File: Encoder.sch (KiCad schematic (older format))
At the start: 7 parts

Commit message: finalizado enrutado provisional
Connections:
- net D2: now also C16.1, R42.2; no longer C15.1, R40.2
- net D5: now also C15.1, R40.2; no longer C16.1, R42.2
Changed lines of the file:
@@
 	3700 2800 3150 2800
 Connection ~ 3150 2800
+Text GLabel 3700 2800 2    50   Output ~ 0
+D2
 Text GLabel 3700 2700 2    50   Output ~ 0
-D2
-Text GLabel 3700 2800 2    50   Output ~ 0
 D5
 $Bitmap

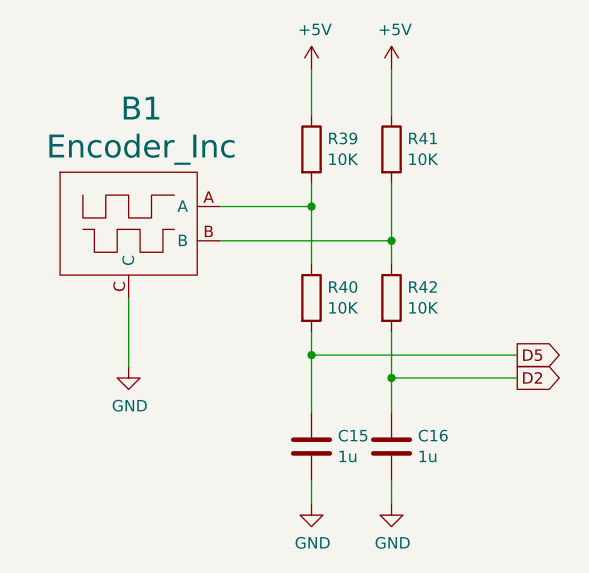
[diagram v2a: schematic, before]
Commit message: corregidos valores en esquema y simbolos corruptos
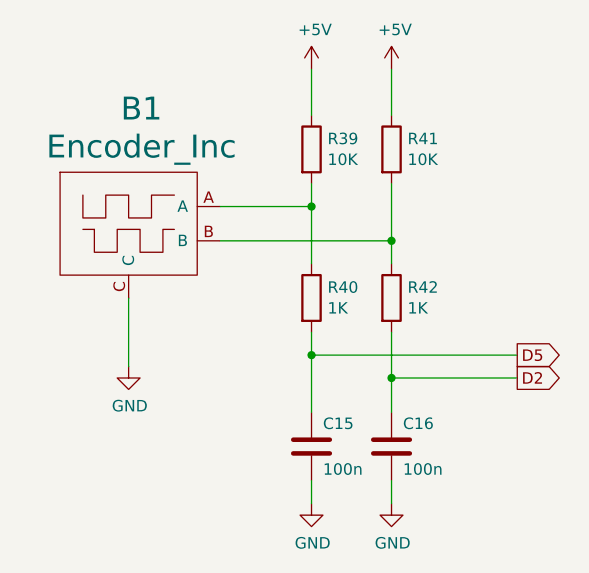
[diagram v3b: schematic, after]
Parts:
- C15: value 1u -> 100n; Ref CL21B105KAFNNNE -> CL21B104KBCNNNC; Ref_Proveedor CL21B105KAFNNNE -> CL21B104KBCNNNC
- C16: value 1u -> 100n; Ref_Proveedor CL21B105KAFNNNE -> CL21B105KAFNNNECL21B104KBCNNNC
- R40, R42: value 10K -> 1K; Ref CRCW080510K0FKEA -> CL21B104KBCNNNC; Ref_Proveedor CRCW080510K0FKEA -> CL21B104KBCNNNC
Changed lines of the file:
@@
 EESchema Schematic File Version 2
+LIBS:Nano_PB-rescue
 LIBS:Interfaces
-LIBS:Nano_PB-rescue
 LIBS:Sensores
 LIBS:power
@@
 LIBS:matriz_led
 LIBS:Pasivos
+LIBS:Reles
 LIBS:Nano_PB-cache
 EELAYER 26 0
@@
 	2000 2450 2000 2750
 $Comp
-L GND #PWR083
+L GND #PWR075
 U 1 1 579DF9A7
 P 2000 2750
-F 0 "#PWR083" H 2000 2500 50  0001 C CNN
+F 0 "#PWR075" H 2000 2500 50  0001 C CNN
 F 1 "GND" H 2005 2577 50  0000 C CNN
 F 2 "" H 2000 2750 50  0000 C CNN
@@
 P 2800 2450
 F 0 "R40" H 2870 2496 50  0000 L CNN
-F 1 "10K" H 2870 2405 50  0000 L CNN
+F 1 "1K" H 2870 2405 50  0000 L CNN
 F 2 "Resistencias:R_0805" V 2730 2450 50  0001 C CNN
 F 3 "" H 2800 2450 50  0000 C CNN
 F 4 "VISHAY" H 4350 1650 60  0001 C CNN "Fabricante"
-F 5 "CRCW080510K0FKEA" H 4350 1650 60  0001 C CNN "Ref"
-F 6 "1/8W" H 4350 1650 60  0001 C CNN "Potencia"
-F 7 "1%" H 4350 1650 60  0001 C CNN "Tolerancia"
-F 8 "TME" H 4350 1650 60  0001 C CNN "Provedor"
-F 9 "CRCW080510K0FKEA" H 4350 1650 60  0001 C CNN "Ref_Proveedor"
+F 5 "CL21B104KBCNNNC" H 4350 1650 60  0001 C CNN "Ref"
+F 6 "1/8W" H 4350 1650 60  0001 C CNN "Potencia"
+F 7 "1%" H 4350 1650 60  0001 C CNN "Tolerancia"
+F 8 "TME" H 4350 1650 60  0001 C CNN "Provedor"
+F 9 "CL21B104KBCNNNC" H 4350 1650 60  0001 C CNN "Ref_Proveedor"
 	1    2800 2450
 	1    0    0    -1
@@
 P 3150 2450
 F 0 "R42" H 3220 2496 50  0000 L CNN
-F 1 "10K" H 3220 2405 50  0000 L CNN
+F 1 "1K" H 3220 2405 50  0000 L CNN
 F 2 "Resistencias:R_0805" V 3080 2450 50  0001 C CNN
 F 3 "" H 3150 2450 50  0000 C CNN
 F 4 "VISHAY" H 4350 1650 60  0001 C CNN "Fabricante"
-F 5 "CRCW080510K0FKEA" H 4350 1650 60  0001 C CNN "Ref"
-F 6 "1/8W" H 4350 1650 60  0001 C CNN "Potencia"
-F 7 "1%" H 4350 1650 60  0001 C CNN "Tolerancia"
-F 8 "TME" H 4350 1650 60  0001 C CNN "Provedor"
-F 9 "CRCW080510K0FKEA" H 4350 1650 60  0001 C CNN "Ref_Proveedor"
+F 5 "CL21B104KBCNNNC" H 4350 1650 60  0001 C CNN "Ref"
+F 6 "1/8W" H 4350 1650 60  0001 C CNN "Potencia"
+F 7 "1%" H 4350 1650 60  0001 C CNN "Tolerancia"
+F 8 "TME" H 4350 1650 60  0001 C CNN "Provedor"
+F 9 "CL21B104KBCNNNC" H 4350 1650 60  0001 C CNN "Ref_Proveedor"
 	1    3150 2450
 	1    0    0    -1
@@
 U 1 1 579DFAC3
 P 2800 3100
-F 0 "C15" H 2915 3146 50  0000 L CNN
-F 1 "1u" H 2915 3055 50  0000 L CNN
+F 0 "C15" H 2850 3200 50  0000 L CNN
+F 1 "100n" H 2850 3000 50  0000 L CNN
 F 2 "Capacitors_SMD:C_0805" H 2838 2950 50  0001 C CNN
 F 3 "" H 2800 3100 50  0000 C CNN
 F 4 "SAMSUNG" H 2800 3100 60  0001 C CNN "Fabricante"
-F 5 "CL21B105KAFNNNE" H 2800 3100 60  0001 C CNN "Ref"
+F 5 "CL21B104KBCNNNC" H 2800 3100 60  0001 C CNN "Ref"
 F 6 "~" H 2800 3100 60  0001 C CNN "Potencia"
 F 7 "~" H 2800 3100 60  0001 C CNN "Tolerancia"
 F 8 "TME" H 2800 3100 60  0001 C CNN "Provedor"
-F 9 "CL21B105KAFNNNE" H 2800 3100 60  0001 C CNN "Ref_Proveedor"
+F 9 "CL21B104KBCNNNC" H 2800 3100 60  0001 C CNN "Ref_Proveedor"
 	1    2800 3100
 	1    0    0    -1
@@
 U 1 1 579DFAF3
 P 3150 3100
-F 0 "C16" H 3265 3146 50  0000 L CNN
-F 1 "1u" H 3265 3055 50  0000 L CNN
+F 0 "C16" H 3200 3200 50  0000 L CNN
+F 1 "100n" H 3200 3000 50  0000 L CNN
 F 2 "Capacitors_SMD:C_0805" H 3188 2950 50  0001 C CNN
 F 3 "" H 3150 3100 50  0000 C CNN
@@
 F 7 "~" H 3150 3100 60  0001 C CNN "Tolerancia"
 F 8 "TME" H 3150 3100 60  0001 C CNN "Provedor"
-F 9 "CL21B105KAFNNNE" H 3150 3100 60  0001 C CNN "Ref_Proveedor"
+F 9 "CL21B105KAFNNNECL21B104KBCNNNC" H 3150 3100 60  0001 C CNN "Ref_Proveedor"
 	1    3150 3100
 	1    0    0    -1
@@
 	2800 2600 2800 2950
 $Comp
-L GND #PWR084
+L GND #PWR076
 U 1 1 579DFBCA
 P 2800 3350
-F 0 "#PWR084" H 2800 3100 50  0001 C CNN
+F 0 "#PWR076" H 2800 3100 50  0001 C CNN
 F 1 "GND" H 2805 3177 50  0000 C CNN
 F 2 "" H 2800 3350 50  0000 C CNN
@@
 $EndComp
 $Comp
-L GND #PWR085
+L GND #PWR077
 U 1 1 579DFBEA
 P 3150 3350
-F 0 "#PWR085" H 3150 3100 50  0001 C CNN
+F 0 "#PWR077" H 3150 3100 50  0001 C CNN
 F 1 "GND" H 3155 3177 50  0000 C CNN
 F 2 "" H 3150 3350 50  0000 C CNN
@@
 	2800 3350 2800 3250
 $Comp
-L +5V #PWR086
+L +5V #PWR078
 U 1 1 579DFC2A
 P 2800 1450
-F 0 "#PWR086" H 2800 1300 50  0001 C CNN
+F 0 "#PWR078" H 2800 1300 50  0001 C CNN
 F 1 "+5V" H 2815 1623 50  0000 C CNN
 F 2 "" H 2800 1450 50  0000 C CNN
@@
 $EndComp
 $Comp
-L +5V #PWR087
+L +5V #PWR079
 U 1 1 579DFC51
 P 3150 1450
-F 0 "#PWR087" H 3150 1300 50  0001 C CNN
+F 0 "#PWR079" H 3150 1300 50  0001 C CNN
 F 1 "+5V" H 3165 1623 50  0000 C CNN
 F 2 "" H 3150 1450 50  0000 C CNN
@@
 $Bitmap
 Pos 7500 4400
-Scale 0,350000
+Scale 0,000000
 Data
 89 50 4E 47 0D 0A 1A 0A 00 00 00 0D 49 48 44 52 00 00 01 D5 00 00 01 ED 08 06 00 00 00 4F 90 E4
